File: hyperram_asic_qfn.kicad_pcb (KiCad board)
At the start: 4 copper layers, 79.5 x 70 mm, 53 parts, among them IC1 W25Q32JVSSIQ_TR, IC2 S27KL0641DABHI020, IC5 LP5907MFX-3.3_NOPB, IC6 MCP1824T-1802E_OT, J1 USB_B_Micro, J2 Conn_02x06_Odd_Even, J3 1156915, J4 1156915, J7 Conn_02x10_Odd_Even, U1 CARAVEL_QFN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

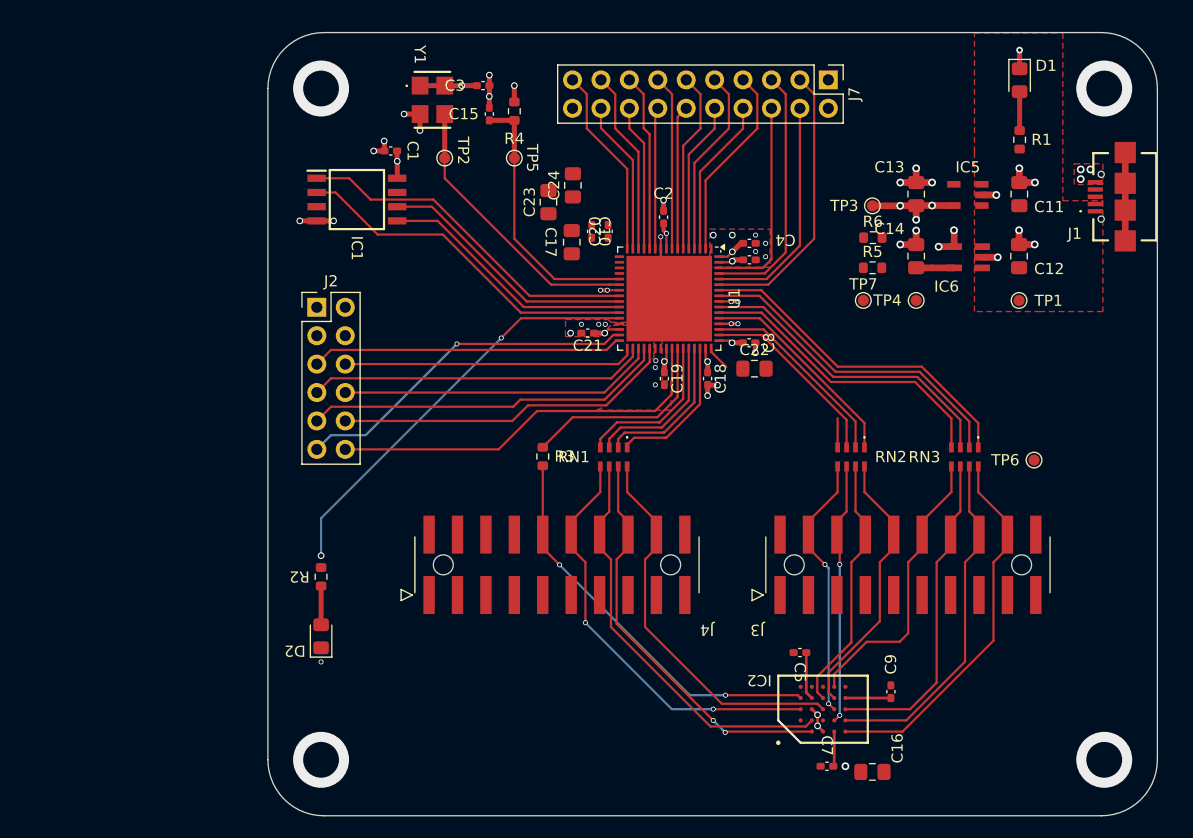
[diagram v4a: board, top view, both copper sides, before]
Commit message: All signals routed, polygons filled.
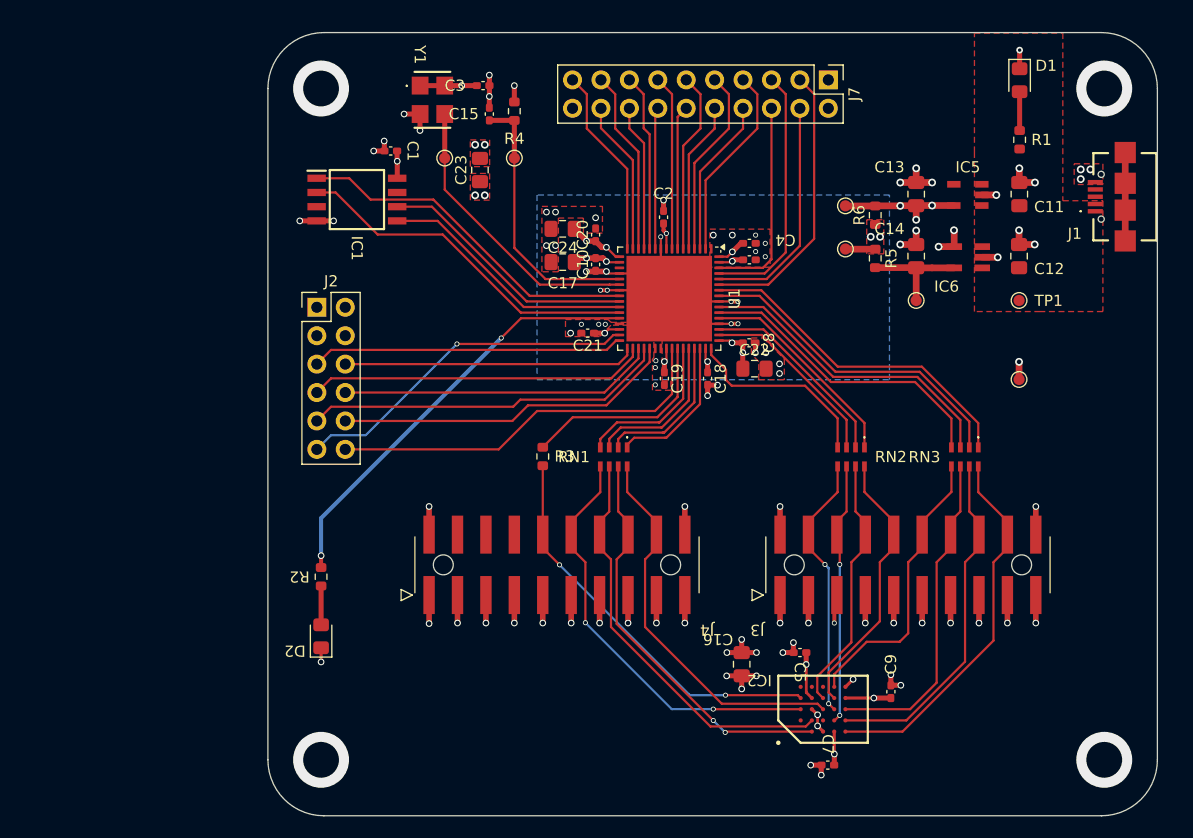
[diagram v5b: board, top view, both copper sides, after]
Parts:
- moved C16 15.1 mm to (164.8, 125.8), turned to 90 degrees
- moved TP6 7.33 mm to (189.6, 100.3)
- moved C23 6.76 mm to (141.5, 81.6)
- moved TP7 4.87 mm to (174.1, 88.6)
- moved C24 3.99 mm to (148.8, 86.8), turned to 180 degrees
- moved C10 2.98 mm to (151.8, 90.0), turned to -90 degrees
- moved TP3 2.41 mm to (174.1, 84.8)
- moved R6 2.02 mm to (176.8, 85.6), turned to 90 degrees
- moved C17 1.95 mm to (148.8, 89.8), turned to 180 degrees
- moved C20 1.16 mm to (151.8, 87.4)
- moved R5 0.87 mm to (176.8, 89.5), turned to -90 degrees
- moved C7 0.13 mm to (172.5, 134.8)
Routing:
- net GND: track 47.1 -> 142.6 mm, vias 56 -> 103
- net /cvl_hr_dq0: track 4.82 -> 17.4 mm
- net +3V3: track 40.8 -> 52.0 mm, vias 11 -> 21
- net VCC: track 4.44 -> 13.8 mm, vias 2 -> 7
- net +1V8: track 3.40 -> 9.99 mm
- net /gpio: track 37.4 -> 38.5 mm
- net /clock: track 25.3 -> 25.9 mm
- net (no net): vias 1 -> 0
- added copper zone on F.Cu, net +3V3
- added copper zone on B.Cu, net VCC
- added copper zone on F.Cu, net VCC

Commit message: Fixed PCB DRC issues - prepared for PCBWay, track/spacing 4/4mils, min hole size 0.25mm
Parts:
- moved C2 0.15 mm to (157.9, 85.6)
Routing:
- net unconnected-(J1-Shield-Pad6)_2: track 0.00 -> 7.90 mm
- net (no net): track 7.90 -> 0.00 mm
- net GND: track 142.6 -> 143.1 mm, vias 103 -> 102

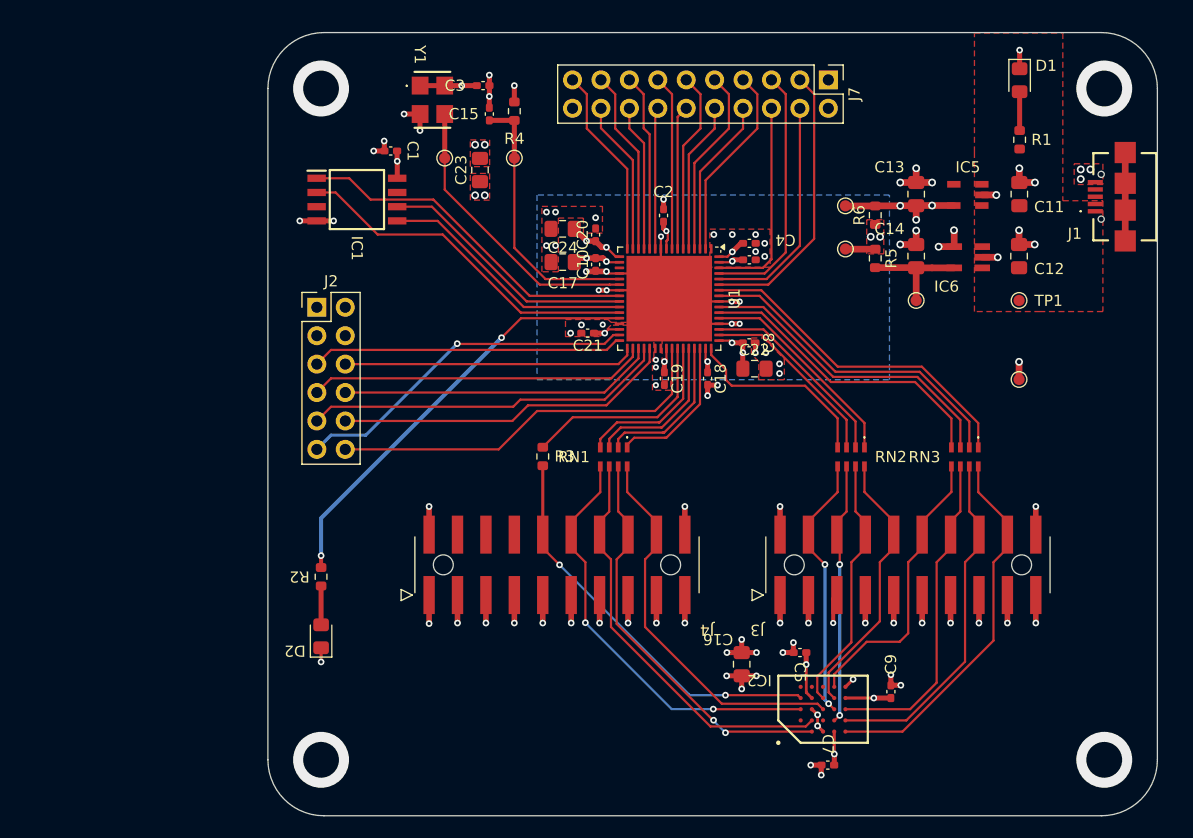
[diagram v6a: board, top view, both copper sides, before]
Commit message: Adjusted References on Silkscreen for better readability
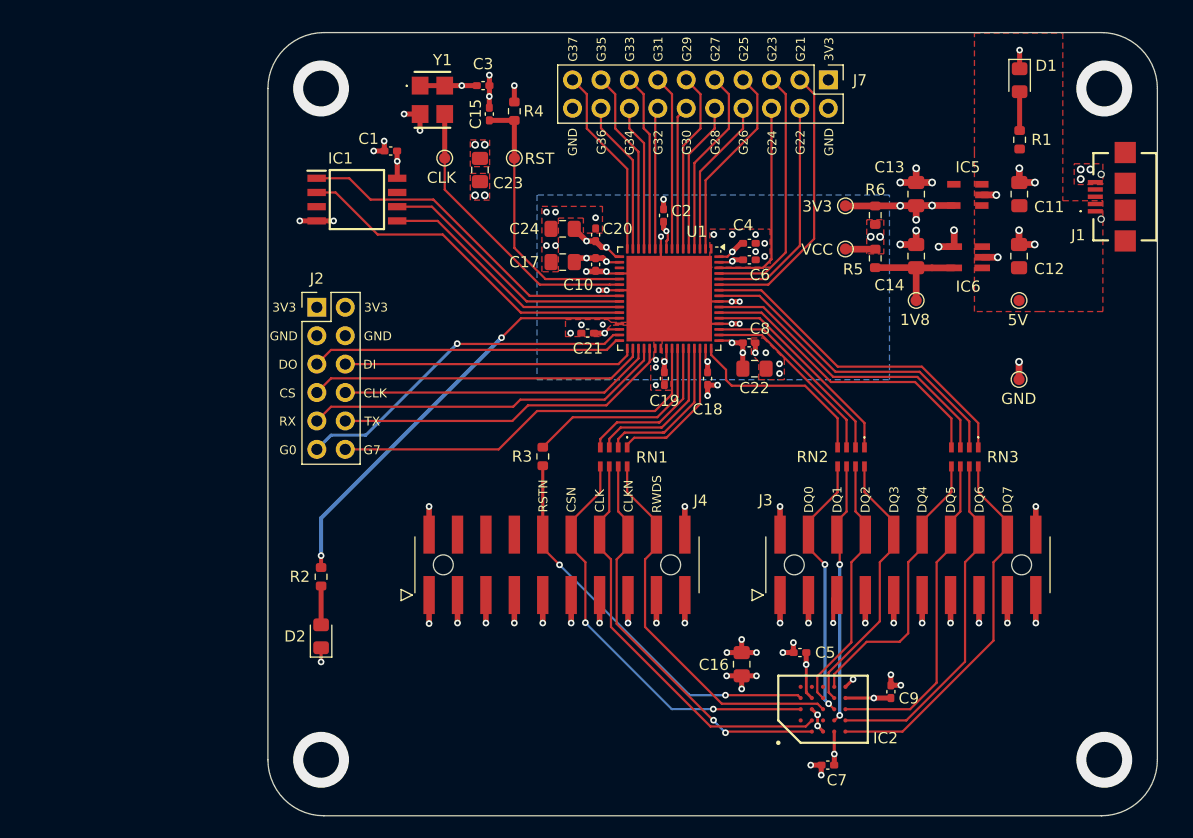
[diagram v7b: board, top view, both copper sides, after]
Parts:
- TP1: value TestPoint -> 5V
- TP2: value CLOCK -> CLK
- TP3: value TestPoint -> 3V3
- TP4: value TestPoint -> 1V8
- TP6: value TestPoint -> GND
- TP7: value TestPoint -> VCC
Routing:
- net unconnected-(J1-Shield-Pad6)_1: track 7.90 -> 0.00 mm
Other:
- board text added: "1V8"
- board text added: "3V3"
- board text added: "5V"
- board text added: "CLK"
- board text added: "CLKN"
- board text added: "CS"
- board text added: "CSN"
- board text added: "DI"
- board text added: "DO"
- board text added: "DQ0"
- board text added: "DQ1"
- board text added: "DQ2"
- board text added: "DQ3"
- board text added: "DQ4"
- board text added: "DQ5"
- board text added: "DQ6"
- board text added: "DQ7"
- board text added: "G0"
- board text added: "G21"
- board text added: "G22"
- board text added: "G23"
- board text added: "G24"
- board text added: "G25"
- board text added: "G26"
- board text added: "G27"
- board text added: "G28"
- board text added: "G29"
- board text added: "G30"
- board text added: "G31"
- board text added: "G32"
- board text added: "G33"
- board text added: "G34"
- board text added: "G35"
- board text added: "G36"
- board text added: "G37"
- board text added: "G7"
- board text added: "GND"
- board text added: "RST"
- board text added: "RSTN"
- board text added: "RWDS"
- board text added: "RX"
- board text added: "TX"
- board text added: "VCC"

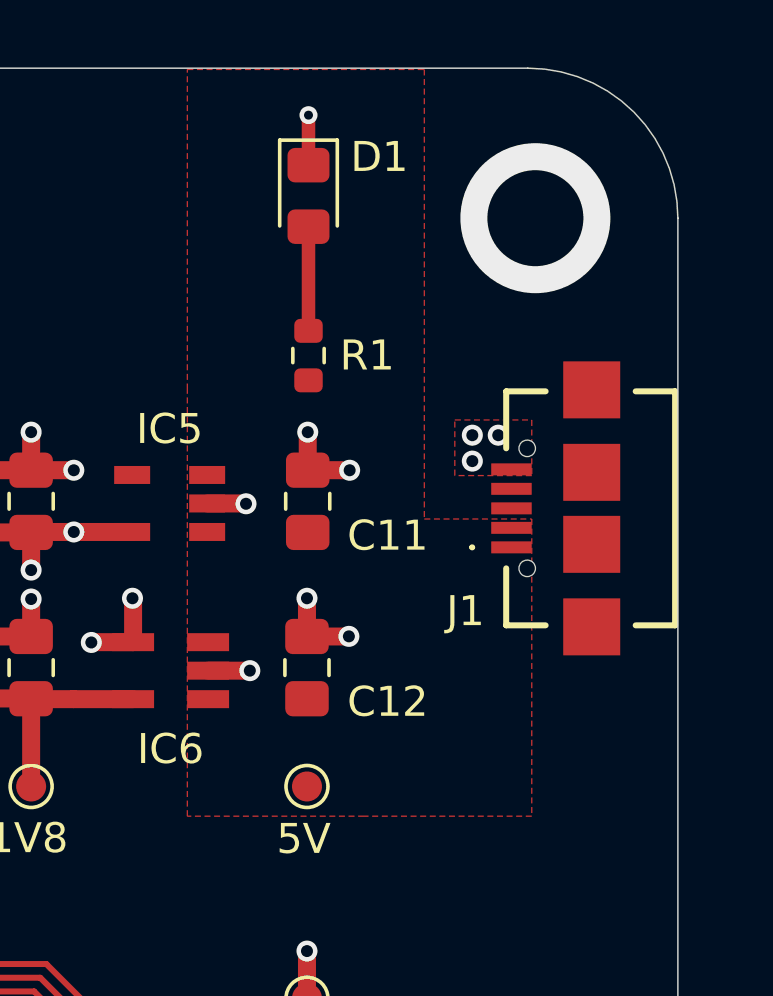
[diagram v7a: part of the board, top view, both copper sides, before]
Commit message: Fixed position of USB connector
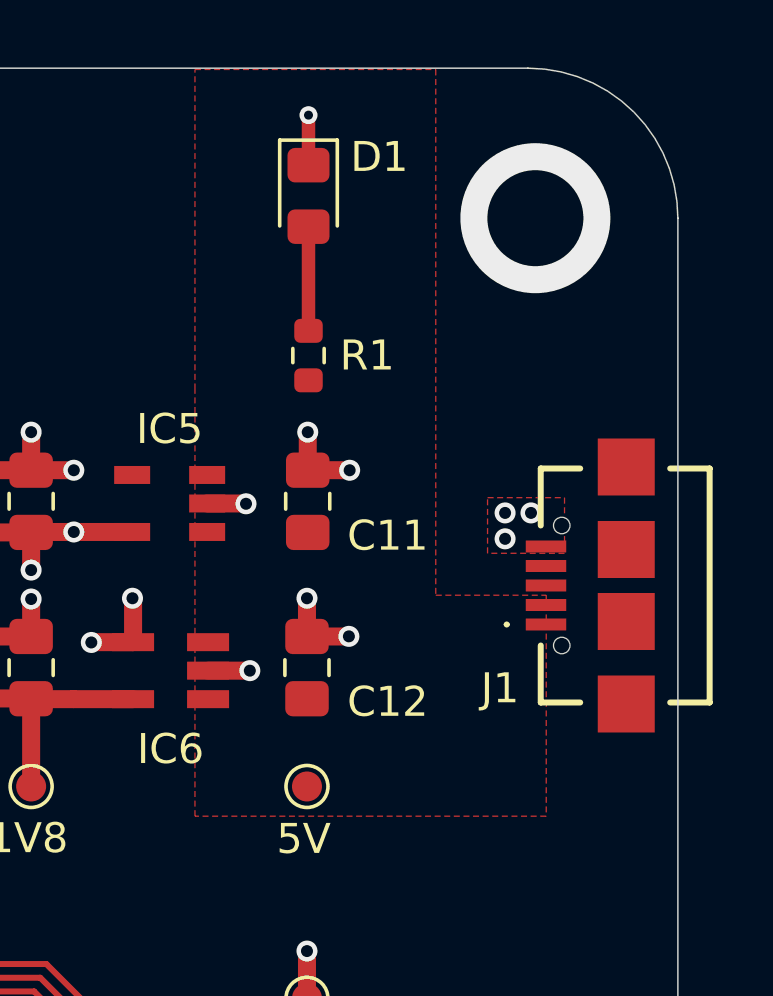
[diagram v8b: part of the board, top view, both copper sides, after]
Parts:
- moved J1 2.82 mm to (200.2, 86.5)
